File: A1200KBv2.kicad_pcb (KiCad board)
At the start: 2 copper layers, 450 x 125 mm, 145 parts, among them J1 Conn_01x32_Female, K1 ESC, K10 L.BLANK, K11 F1, K12 L.AMIGA, K13 2, K14 W, K15 A, K16 Z, K17 F2, K18 3, K19 E, K2 TILDE, K20 S, K21 X, K22 F3, K23 4, K24 R, K25 D, K26 C, K27 F4, K28 5, K29 T, K3 TAB, K30 F, K31 V, K32 SPACE SWITCH, K33 F5, K34 6, K35 Y, K36 G, K37 B, K38 7, K39 U, K4 CTRL, K40 H, K41 N, K42 F6, K43 8, K44 I, K45 J, K46 M, K47 9, K48 O, K49 K, K5 L.SHIFT, K50 LESSTHAN, K51 F7, K52 0, K53 P, K54 L, K55 GRTRTHAN, K56 F8, K57 MINUS, K58 L.CURLY, K59 COLON, K6 L.ALT, K60 QUESTION, K61 R.AMIGA, K62 F9, K63 PLUS, K64 R.CURLY, K65 ", K66 R.SHIFT, K67 R.ALT, K68 F10, K69 PIPE, K7 1, K70 R.BLANK, K71 RETURN, K72 BS, K73 LEFT, K74 DEL, K75 UP, K76 DOWN, K77 HELP, K78 RIGHT, K79 NUM_(, K8 Q, K80 NUM_7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

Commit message: New version with new footprints; low-profile plate stabilizers
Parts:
- removed the ? at (300.7, 79.4)
- removed the ? at (281.5, 128.1)
- removed the ? at (305.3, 128.1)
- removed the ? at (315.9, 103.3)
- removed the ? at (426.1, 130.5)
- removed the ? at (402.3, 145.8)
- removed the ? at (281.5, 112.8)
- removed the ? at (453.4, 141.2)
- removed the ? at (426.1, 145.8)
- removed the ? at (300.7, 103.3)
- removed the ? at (31.3, 74.7)
- removed the ? at (468.7, 117.4)
- removed the ? at (315.9, 79.4)
- removed the ? at (305.3, 112.8)
- removed the ? at (55.1, 90.0)
- removed the ? at (468.7, 141.2)
- removed the ? at (402.3, 130.5)
- removed the ? at (469.0, 146.0)
- removed the ? at (55.1, 74.7)
- removed the ? at (31.3, 90.0)
- removed the ? at (469.0, 111.0)
- removed the ? at (453.4, 117.4)
- removed the ? at (461.0, 112.0)
- K3, K83, K96: footprint key-switches.pretty-0.11.0:SW_Gateron_LowProfile_THT -> Amiga_FFC:KS-33-2U-plate-stabilizer
- K66: footprint key-switches.pretty-0.11.0:SW_Gateron_LowProfile_THT -> Amiga_FFC:KS-33-2.75U-plate-stabilizer
- K71: footprint key-switches.pretty-0.11.0:SW_Gateron_LowProfile_THT -> Amiga_FFC:KS-33-ISO-plate-stabilizer
- moved ? 56.6 mm to (469.0, 112.0)
- moved ? 11.2 mm to (388.0, 66.0)
- moved ? 5.00 mm to (26.0, 50.0)
- turned K96 to 90 degrees
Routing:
- net /3: track 480.7 -> 507.5 mm
- net /4: track 609.2 -> 631.9 mm
- net /24: track 427.5 -> 436.9 mm
- net /14: track 268.3 -> 260.6 mm
- net (no net): track 7.00 -> 0.00 mm
- net /20: track 456.4 -> 462.6 mm
- net /1: track 402.3 -> 408.2 mm
- net /11: track 206.2 -> 210.8 mm
- net /6: track 208.1 -> 212.5 mm, vias 1 -> 2
- net /5: track 383.5 -> 381.3 mm
- net Net-(D1-K): track 273.5 -> 275.1 mm
- net Net-(D1-A): track 251.4 -> 252.8 mm
- net /28: track 385.8 -> 384.5 mm
- net /26: track 293.7 -> 292.5 mm
- net /16: track 639.9 -> 640.8 mm
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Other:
- board text added: "8U"
- board text added: "9U"
- board text added: "MOUNT CONNECTOR OTHER SIDE!"
- board text added: "PIN 1"

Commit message: fab 9/7/24 A1200 for KS-33 A1200.net case
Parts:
- removed ? (x21): , 
- removed D1, D2, D3, D4: LED, LED_SMD:LED_0805_2012Metric_Pad1.15x1.40mm_HandSolder
- added C1: .01uF, Capacitor_SMD:C_0805_2012Metric_Pad1.18x1.45mm_HandSolder, F.Cu at (443.0, 47.5)
- added D6: CAPS LED (BLUE), LED_SMD:LED_0805_2012Metric, F.Cu at (465.4, 42.3)
- added D7: POWER LED (RED), LED_SMD:LED_0805_2012Metric, F.Cu at (468.9, 42.3)
- added D8: FLOPPY LED (ORANGE), LED_SMD:LED_0805_2012Metric, F.Cu at (467.2, 50.3)
- added D9: DISK LED (GREEN), LED_SMD:LED_0805_2012Metric, F.Cu at (467.2, 58.3)
- added J2: LED HDR, Connector_PinHeader_2.54mm:PinHeader_1x04_P2.54mm_Vertical, F.Cu at (440.3, 43.0)
- added R1: CAPS, Resistor_SMD:R_0805_2012Metric_Pad1.20x1.40mm_HandSolder, F.Cu at (461.9, 42.3)
- added R2: PWR, Resistor_SMD:R_0805_2012Metric_Pad1.20x1.40mm_HandSolder, F.Cu at (472.5, 42.3)
- added R3: 0R, Resistor_SMD:R_0805_2012Metric_Pad1.20x1.40mm_HandSolder, F.Cu at (445.5, 47.5)
- added R4: FLOPPY, Resistor_SMD:R_0805_2012Metric_Pad1.20x1.40mm_HandSolder, F.Cu at (463.6, 50.3)
- added R5: DISK, Resistor_SMD:R_0805_2012Metric_Pad1.20x1.40mm_HandSolder, F.Cu at (463.6, 58.3)
- added U1: 74LVC2GU04, Package_TO_SOT_SMD:SOT-23-6, F.Cu at (446.1, 43.0)
- K1, K10, K13, K14, K15, K16, K18, K19, K20, K21, K23, K24, K25, K26, K28, K29, K30, K31, K34, K35, K36, K37, K38, K39, K40, K41, K43, K44, K45, K46, K47, K48, K49, K50, K52, K53, K54, K55, K57, K58, K59, K60, K63, K64, K65, K69, K7, K70, K72, K73, K75, K76, K78, K79, K8, K80, K81, K82, K84, K85, K86, K87, K88, K89, K90, K91, K92, K93, K94, K95: footprint key-switches.pretty-0.11.0:SW_Gateron_LowProfile_THT -> Amiga Keyboard:Gateron-KS33-Solderable-1U
- K11, K12, K17, K22, K27, K33, K4, K42, K51, K56, K6, K61, K62, K67, K68: footprint key-switches.pretty-0.11.0:SW_Gateron_LowProfile_THT -> Amiga Keyboard:Gateron-KS33-Solderable-1.25U
- K2, K74, K77: footprint key-switches.pretty-0.11.0:SW_Gateron_LowProfile_THT -> Amiga Keyboard:Gateron-KS33-Solderable-1.5U
- K3, K83, K96: footprint Amiga_FFC:KS-33-2U-plate-stabilizer -> Amiga Keyboard:KS-33-2U-stabilizer
- K32: footprint Amiga_FFC:KS-33-Universal-Space -> Amiga Keyboard:KS-33-8U-space
- K5: footprint key-switches.pretty-0.11.0:SW_Gateron_LowProfile_THT -> Amiga Keyboard:Gateron-KS33-Solderable-1.75U
- K66: footprint Amiga_FFC:KS-33-2.75U-plate-stabilizer -> Amiga Keyboard:KS-33-2U-stabilizer
- K71: footprint Amiga_FFC:KS-33-ISO-plate-stabilizer -> Amiga Keyboard:KS-33-ISO-2U-stabilizer
- K9: footprint key-switches.pretty-0.11.0:SW_Gateron_LowProfile_THT -> Amiga Keyboard:Gateron-KS33-LED-Solderable-1U
- moved K79 23.7 mm to (421.6, 79.1)
- moved K80 23.7 mm to (421.6, 98.1)
- moved K82 23.7 mm to (421.6, 136.2)
- moved K63 23.7 mm to (288.9, 79.2)
- moved K68 23.7 mm to (305.4, 50.5)
- moved K53 23.7 mm to (260.2, 98.2)
- moved K65 23.7 mm to (284.3, 117.3)
- moved K81 23.7 mm to (421.6, 117.2)
- moved K67 23.7 mm to (309.9, 155.4)
- moved K10 23.7 mm to (84.1, 136.3)
- moved K11 23.7 mm to (81.9, 50.4)
- moved K22 23.7 mm to (129.6, 50.5)
- moved K26 23.7 mm to (141.3, 136.3)
- moved K29 23.7 mm to (164.9, 98.3)
- moved K37 23.7 mm to (179.4, 136.3)
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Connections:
- J1 pad 31: Net-(D1-K) -> /CAPSLOCK
- J1 pad 9: Net-(D1-A) -> /LED
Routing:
- net /CAPSLOCK: track 0.00 -> 438.7 mm, vias 0 -> 3
- net Net-(D1-K): track 275.1 -> 0.00 mm, vias 3 -> 0
- net Net-(D1-A): track 252.8 -> 0.00 mm, vias 3 -> 0
- net /LED: track 0.00 -> 172.8 mm, vias 0 -> 2
- net Net-(D8-K): track 0.00 -> 61.3 mm, vias 0 -> 1
- net /LEDs/PWRLED: track 0.00 -> 51.0 mm
- net Net-(J2-Pin_3): track 0.00 -> 39.6 mm
- net Net-(J2-Pin_4): track 0.00 -> 36.2 mm
- net Net-(D6-K): track 0.00 -> 27.6 mm, vias 0 -> 2
- net Net-(D7-K): track 0.00 -> 25.8 mm
- net /30: track 507.3 -> 523.7 mm
- net /11: track 210.8 -> 223.3 mm, vias 1 -> 2
- net /27: track 450.2 -> 462.4 mm
- net /14: track 260.6 -> 251.1 mm
- net /13: track 251.8 -> 260.2 mm, vias 1 -> 2
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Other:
- outline, holes or cut-outs redrawn
- board text added: "115"
- board text added: "225"
- board text added: "335"
- board text added: "445"
- board text added: "5"
- board text added: "A"
- board text added: "CAPS (BLUE)"
- board text added: "CR"
- board text added: "DISK (GREEN)"
- board text added: "FIT R3, OMIT U1, D6 etc. FOR NORMAL LED OPERATION FIT ALL BUT R3 FOR BICOLOR POWER LED CAPS INDICATOR"
- board text added: "FLOPPY (ORANGE)"
- board text added: "K"
- board text added: "L. SHIFT"
- board text added: "Mechanical keyboard for the A1200 - A1200KBv2 r3 for Gateron KS-33 low-profile switches, A1200.net case aeberbach 07/24 grayunicorn.com LICENSE: CC BY-NC-SA 4.0"
- board text added: "NUM_0"
- board text added: "NUM_ENTER"
- board text added: "POWER (RED)"
- board text added: "R_SHIFT"
- board text added: "SPACE"
- board text added: "TAB"
- board text removed: "6.25U"
- board text removed: "7U"
- board text removed: "8/9U"
- board text removed: "8U"
- board text removed: "Mechanical keyboard for the A1200 - A1200KBv2 for Gateron KS-33 low-profile switches (mount one 0805 LED for caps lock in preferred location) aeberbach 06/24 grayunicorn.com LICENSE: CC BY-NC-SA 4.0"

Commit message: Current
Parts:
- moved K32 0.36 mm to (187.9, 155.3)
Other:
- board text added: "Mechanical keyboard for the A1200 - A1200KBv2 r4 for Gateron KS-33 low-profile switches, A1200.net case aeberbach 07/24 grayunicorn.com LICENSE: CC BY-NC-SA 4.0"
- board text removed: "Mechanical keyboard for the A1200 - A1200KBv2 r3 for Gateron KS-33 low-profile switches, A1200.net case aeberbach 07/24 grayunicorn.com LICENSE: CC BY-NC-SA 4.0"
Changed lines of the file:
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@@
 		(tags "LED")
 		(property "Reference" "D9"
-			(at 0 2.171855 360)
+			(at 0 2.171855 0)
 			(layer "F.SilkS")
 			(effects
@@
 		)
 		(property "Value" "DISK LED (GREEN)"
-			(at 0 2.671855 360)
+			(at 0 2.671855 0)
 			(layer "F.Fab")
 			(hide yes)
@@
 		(tags "resistor handsolder")
 		(property "Reference" "R4"
-			(at 0 -1.65 360)
+			(at 0 -1.65 0)
 			(layer "F.SilkS")
 			(hide yes)
@@
 		)
 		(property "Value" "FLOPPY"
-			(at 0 1.65 360)
+			(at 0 1.65 0)
 			(layer "F.Fab")
 			(hide yes)
@@
 		(tags "resistor handsolder")
 		(property "Reference" "R1"
-			(at 0 -2.198443 360)
+			(at 0 -2.198443 0)
 			(layer "F.SilkS")
 			(hide yes)
@@
 		)
 		(property "Value" "CAPS"
-			(at 0 1.65 360)
+			(at 0 1.65 0)
 			(layer "F.Fab")
 			(hide yes)
@@
 		(locked yes)
 		(layer "F.Cu")
-		(at 188.2728 155.3704)
+		(at 187.92105 155.2954)
 		(property "Reference" "K32"
-			(at 10 -7.5 0)
+			(at 9.2965 -7.65 0)
 			(unlocked yes)
 			(layer "F.SilkS")
@@
 		)
 		(property "Value" "SPACE SWITCH"
-			(at 14.5 -1 0)
+			(at 13.7965 -1.15 0)
 			(unlocked yes)
 			(layer "F.Fab")
@@
 		(attr smd)
 		(fp_line
-			(start -75.84825 -9.45)
-			(end -75.84825 9.6)
+			(start -76.2 -9.525)
+			(end -76.2 9.525)
 			(stroke
 				(width 0.15)
@@
 		)
 		(fp_line
-			(start -75.84825 -9.45)
-			(end 76.55175 -9.45)
+			(start -76.2 -9.525)
+			(end 76.2 -9.525)
 			(stroke
 				(width 0.15)
@@
 		)
 		(fp_line
-			(start -75.84825 9.6)
-			(end 76.55175 9.6)
+			(start -76.2 9.525)
+			(end 76.2 9.525)
 			(stroke
 				(width 0.15)
@@
 		)
 		(fp_line
-			(start -6.64825 -6.925)
-			(end -6.64825 -4.925)
+			(start -7 -7)
+			(end -7 -5)
 			(stroke
 				(width 0.15)
@@
 		)
 		(fp_line
-			(start -6.64825 5.075)
-			(end -6.64825 7.075)
+			(start -7 5)
+			(end -7 7)
 			(stroke
 				(width 0.15)
@@
 		)
 		(fp_line
-			(start -6.64825 7.075)
-			(end -4.64825 7.075)
+			(start -7 7)
+			(end -5 7)
 			(stroke
 				(width 0.15)
@@
 		)
 		(fp_line
-			(start -4.64825 -6.925)
-			(end -6.64825 -6.925)
+			(start -5 -7)
+			(end -7 -7)
 			(stroke
 				(width 0.15)
@@
 		)
 		(fp_line
-			(start 5.35175 -6.925)
-			(end 7.35175 -6.925)
+			(start 5 -7)
+			(end 7 -7)
 			(stroke
 				(width 0.15)
@@
 		)
 		(fp_line
-			(start 5.35175 7.075)
-			(end 7.35175 7.075)
+			(start 5 7)
+			(end 7 7)
 			(stroke
 				(width 0.15)
@@
 		)
 		(fp_line
-			(start 7.35175 -6.925)
-			(end 7.35175 -4.925)
+			(start 7 -7)
+			(end 7 -5)
 			(stroke
 				(width 0.15)
@@
 		)
 		(fp_line
-			(start 7.35175 7.075)
-			(end 7.35175 5.075)
+			(start 7 7)
+			(end 7 5)
 			(stroke
 				(width 0.15)
@@
 		)
 		(fp_line
-			(start 76.55175 -9.45)
-			(end 76.55175 9.6)
+			(start 76.2 -9.525)
+			(end 76.2 9.525)
 			(stroke
 				(width 0.15)
@@
 		)
 		(fp_rect
-			(start -2.84825 -6.225)
-			(end 2.15175 -3.975)
+			(start -3.2 -6.3)
+			(end 1.8 -4.05)
 			(stroke
 				(width 0.1)
@@
 		)
 		(fp_rect
-			(start -69.14825 -8.925)
-			(end -63.14825 6.075)
+			(start -69.75 -9)
+			(end -63.75 6)
 			(stroke
 				(width 0.05)
@@
 		)
 		(fp_rect
-			(start 63.85175 -8.925)
-			(end 69.85175 6.075)
+			(start 63.75 -9)
+			(end 69.75 6)
 			(stroke
 				(width 0.05)
@@
 		)
 		(fp_text user "${REFERENCE}"
-			(at 13.5 -5.5 0)
+			(at 12.7965 -5.65 0)
 			(unlocked yes)
 			(layer "F.Fab")
@@
 		)
 		(pad "" np_thru_hole circle
-			(at 0.35175 0.075 180)
+			(at 0 0 180)
 			(size 5.1 5.1)
 			(drill 5.1)
@@
 		)
 		(pad "1" thru_hole circle
-			(at -4.04825 4.775 180)
+			(at -4.4 4.7 180)
 			(size 2.3 2.3)
 			(drill 1.45)
@@
 		)
 		(pad "2" thru_hole circle
-			(at 2.95175 5.825 180)
+			(at 2.6 5.75 180)
 			(size 2.3 2.3)
 			(drill 1.45)
@@
 		(tags "resistor handsolder")
 		(property "Reference" "R2"
-			(at 0 -1.65 360)
+			(at 0 -1.65 0)
 			(layer "F.SilkS")
 			(hide yes)
@@
 		)
 		(property "Value" "PWR"
-			(at 0 1.65 360)
+			(at 0 1.65 0)
 			(layer "F.Fab")
 			(hide yes)
@@
 		(tags "SOT TO_SOT_SMD")
 		(property "Reference" "U1"
-			(at -3.6375 -1.05 360)
+			(at -3.6375 -1.05 0)
 			(layer "F.SilkS")
 			(effects
@@
 		)
 		(property "Value" "74LVC2GU04"
-			(at 0 2.4 360)
+			(at 0 2.4 0)
 			(layer "F.Fab")
 			(hide yes)
@@
 		(tags "resistor handsolder")
 		(property "Reference" "R3"
-			(at -3 0 360)
+			(at -3 0 0)
 			(layer "F.SilkS")
 			(effects
@@
 		(tags "LED")
 		(property "Reference" "D6"
-			(at 0.936256 -2.203308 360)
+			(at 0.936256 -2.203308 0)
 			(layer "F.SilkS")
 			(effects
@@
 		)
 		(property "Value" "CAPS LED (BLUE)"
-			(at -5.546203 2.390077 360)
+			(at -5.546203 2.390077 0)
 			(layer "F.Fab")
 			(hide yes)
@@
 		(tags "LED")
 		(property "Reference" "D8"
-			(at 0 2.180936 360)
+			(at 0 2.180936 0)
 			(layer "F.SilkS")
 			(effects
@@
 		)
 		(property "Value" "FLOPPY LED (ORANGE)"
-			(at 0 2.680936 360)
+			(at 0 2.680936 0)
 			(layer "F.Fab")
 			(hide yes)
@@
 	)
 	(gr_rect
-		(start 459.2088 59.572)
-		(end 475.2088 57.072)
+		(start 459.2088 57.072)
+		(end 475.2088 59.572)
 		(locked yes)
 		(stroke
@@
 		)
 	)
-	(gr_text "Mechanical keyboard for the A1200 - A1200KBv2 r3\nfor Gateron KS-33 low-profile switches, A1200.net case\naeberbach 07/24 grayunicorn.com\nLICENSE: CC BY-NC-SA 4.0 "
+	(gr_text "Mechanical keyboard for the A1200 - A1200KBv2 r4\nfor Gateron KS-33 low-profile switches, A1200.net case\naeberbach 07/24 grayunicorn.com\nLICENSE: CC BY-NC-SA 4.0 "
 		(at 375 154.5 0)
 		(layer "F.SilkS")
@@
 	)
 	(gr_text "SPACE"
+		(locked yes)
 		(at 185.5 151 0)
 		(layer "F.SilkS")

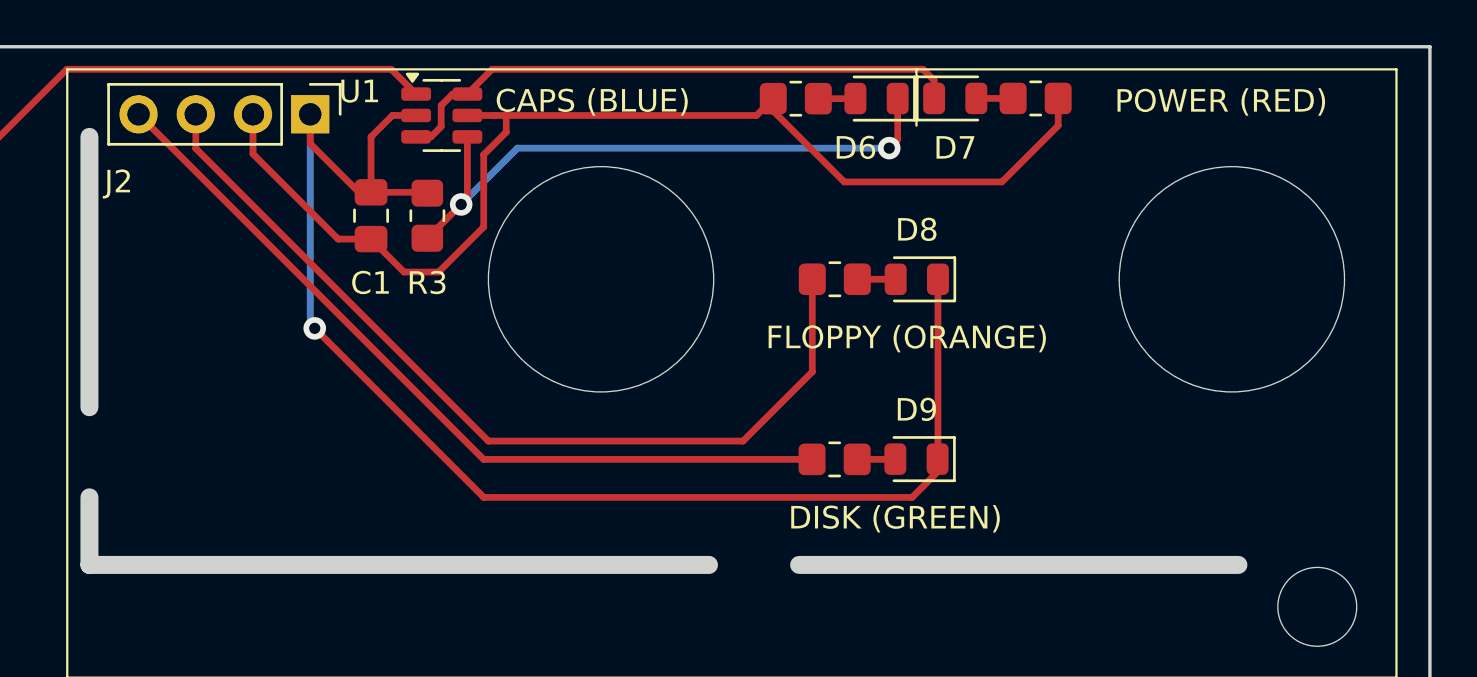
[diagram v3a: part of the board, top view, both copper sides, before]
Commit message: arrange LEDs
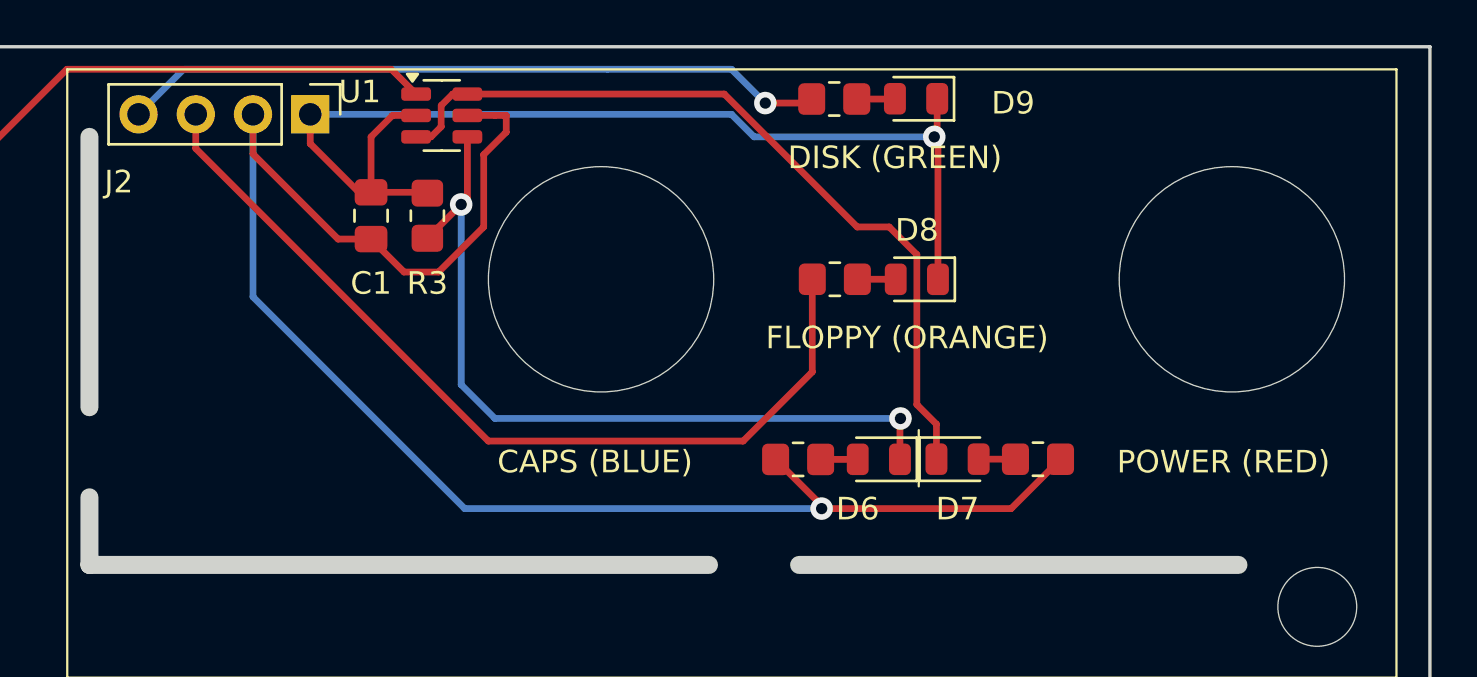
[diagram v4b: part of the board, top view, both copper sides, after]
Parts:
- moved D6 16.0 mm to (465.5, 58.3)
- moved D7 16.0 mm to (469.0, 58.3)
- moved R2 16.0 mm to (472.6, 58.3)
- moved R1 16.0 mm to (462.0, 58.3)
- moved D9 16.0 mm to (467.2, 42.3)
- moved R5 16.0 mm to (463.6, 42.3)
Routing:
- net /LEDs/PWRLED: track 51.0 -> 73.9 mm, vias 0 -> 1
- net Net-(D8-K): track 61.3 -> 48.2 mm
- net Net-(D7-K): track 25.8 -> 36.0 mm
- net Net-(D6-K): track 27.6 -> 35.2 mm
- net Net-(J2-Pin_4): track 36.2 -> 31.4 mm, vias 0 -> 1

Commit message: Plates for final r5
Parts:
- added D1: CAPS_LOCK, LED_SMD:LED_0805_2012Metric, F.Cu at (73.8, 112.1)
- K9: footprint Amiga Keyboard:Gateron-KS33-LED-Solderable-1U -> Amiga Keyboard:Gateron-KS33-Solderable-1U
- moved K32 0.48 mm to (188.4, 155.4)
- moved K83 0.10 mm to (431.2, 155.4)
- moved K92 0.10 mm to (459.7, 155.4)
- moved R2 0.08 mm to (472.7, 58.3)
- moved D7 0.08 mm to (469.1, 58.3)
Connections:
- J1 pad 9: /LED -> VCC
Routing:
- net /LED: track 172.8 -> 0.00 mm, vias 2 -> 0
- net VCC: track 0.00 -> 172.8 mm, vias 0 -> 2
- net /2: track 448.6 -> 468.4 mm
- net /4: track 635.2 -> 627.2 mm, vias 2 -> 1
- net /12: track 229.5 -> 234.7 mm
- net /25: track 329.7 -> 326.4 mm
- net /28: track 379.2 -> 381.3 mm
- net /CAPSLOCK: track 438.7 -> 439.7 mm
- net /10: track 182.1 -> 183.0 mm
- net /11: track 223.3 -> 224.1 mm
- net /27: track 462.4 -> 463.1 mm
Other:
- board text added: "(DNF)"
- board text added: "Mechanical keyboard for the A1200 - A1200KBv2 r5 for Gateron KS-33 low-profile switches aeberbach 08/24 grayunicorn.com LICENSE: CC-BY-NC-SA 4.0"
- board text removed: "Mechanical keyboard for the A1200 - A1200KBv2 r4 for Gateron KS-33 low-profile switches, A1200.net case aeberbach 07/24 grayunicorn.com LICENSE: CC BY-NC-SA 4.0"

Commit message: v6 as manufactured
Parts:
- moved J1 25.7 mm to (192.8, 36.2)
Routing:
- net /4: track 627.2 -> 658.1 mm
- net /2: track 468.4 -> 497.2 mm
- net /3: track 507.8 -> 536.4 mm
- net /1: track 411.5 -> 439.8 mm
- net /28: track 381.3 -> 409.0 mm, vias 3 -> 4
- net /26: track 292.7 -> 320.3 mm, vias 2 -> 3
- net /5: track 384.6 -> 411.8 mm
- net /6: track 208.8 -> 235.7 mm
- net /27: track 463.1 -> 490.0 mm, vias 3 -> 4
- net /8: track 210.6 -> 237.0 mm
- net /24: track 440.6 -> 466.8 mm, vias 3 -> 4
- net /22: track 391.0 -> 416.7 mm
- net /15: track 566.6 -> 592.3 mm
- net /10: track 183.0 -> 208.7 mm
- net /17: track 512.0 -> 537.6 mm
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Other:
- board size 450 x 125 mm -> 450 x 135 mm
- board text added: "Mechanical keyboard for the A1200 - A1200KBv2 r6 for Gateron KS-33 low-profile switches aeberbach 09/24 grayunicorn.com LICENSE: CC-BY-NC-SA 4.0"
- board text removed: "Mechanical keyboard for the A1200 - A1200KBv2 r5 for Gateron KS-33 low-profile switches aeberbach 08/24 grayunicorn.com LICENSE: CC-BY-NC-SA 4.0"
